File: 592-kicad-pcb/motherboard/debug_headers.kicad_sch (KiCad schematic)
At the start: 7 parts, among them J4 Conn_02x06_Odd_Even, J5 Conn_02x06_Odd_Even, J7 Conn_02x06_Odd_Even, J8 Conn_02x06_Odd_Even, J9 Conn_02x06_Odd_Even

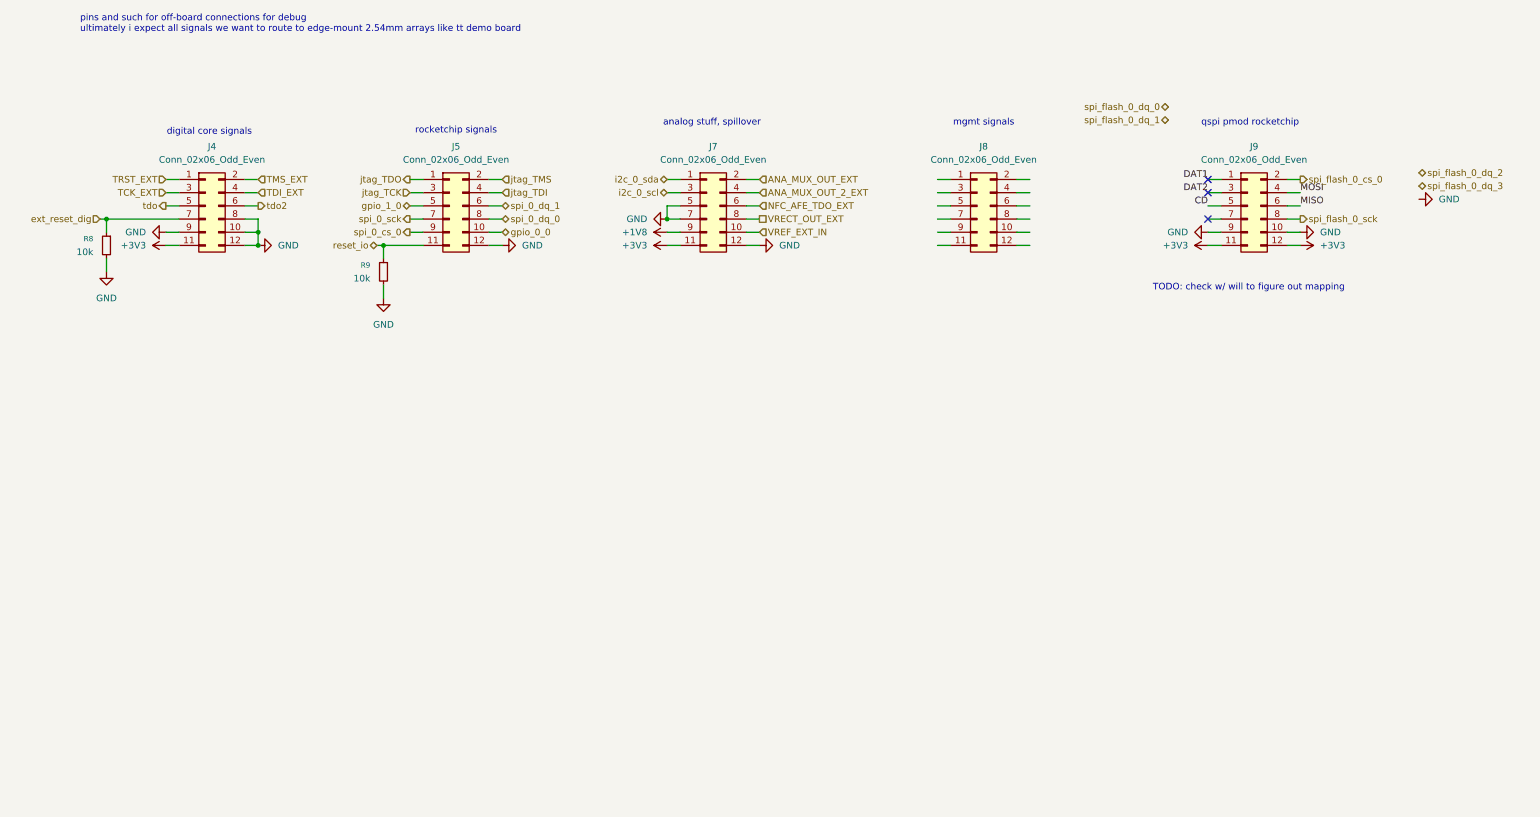
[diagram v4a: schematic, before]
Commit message: clean up some pull up/downs
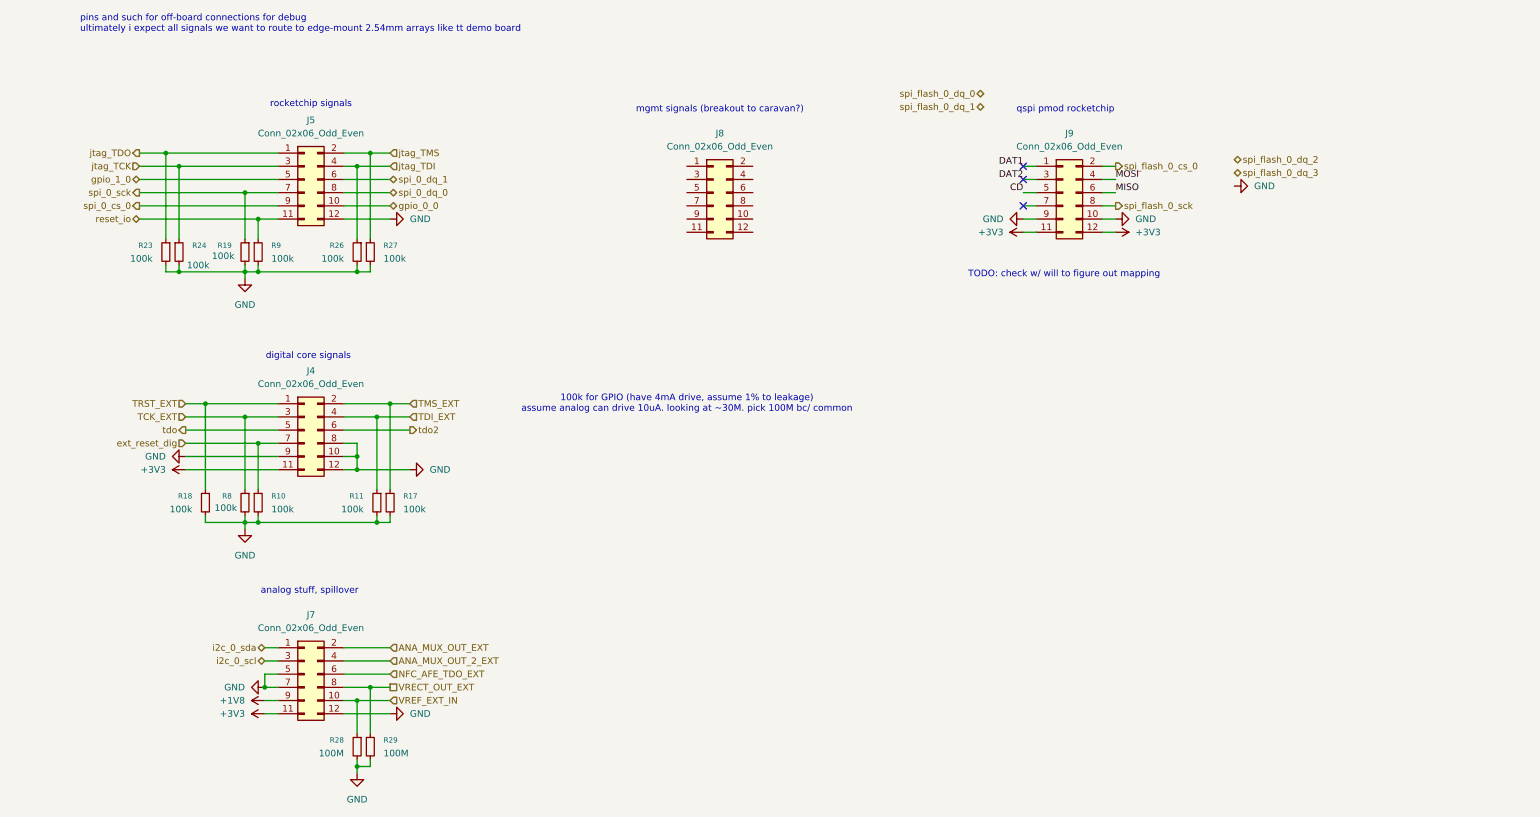
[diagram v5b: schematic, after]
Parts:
- added R10, R11, R17, R18, R19, R23, R24, R26, R27: 100k, Capacitor_SMD:C_0603_1608Metric, symbol Device:R_Small
- added R28, R29: 100M, Capacitor_SMD:C_0603_1608Metric, symbol Device:R_Small
- R8, R9: value 10k -> 100k
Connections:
- net GND: now also R10.2, R11.2, R17.2, R18.2, R19.2, R23.2, R24.2, R26.2, R27.2, R28.2, R29.2
- net TCK_EXT: now also R8.1
- net TDI_EXT: now also R11.1
- net TMS_EXT: now also R17.1
- net TRST_EXT: now also R18.1
- net VRECT_OUT_EXT: now also R29.1
- net VREF_EXT_IN: now also R28.1
- net ext_reset_dig: now also R10.1; no longer R8.1
- net jtag_TCK: now also R24.1
- net jtag_TDI: now also R26.1
- net jtag_TDO: now also R23.1
- net jtag_TMS: now also R27.1
- net spi_0_sck: now also R19.1
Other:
- note added: "100k for GPIO (have 4mA drive, assume 1% to leakage) assume analog can drive 10uA. looking at ~30M. pick 100M bc/ common"
- note added: "mgmt signals (breakout to caravan?)"
- note removed: "mgmt signals"
- moved on the sheet: J4, J5, J7, J8, J9

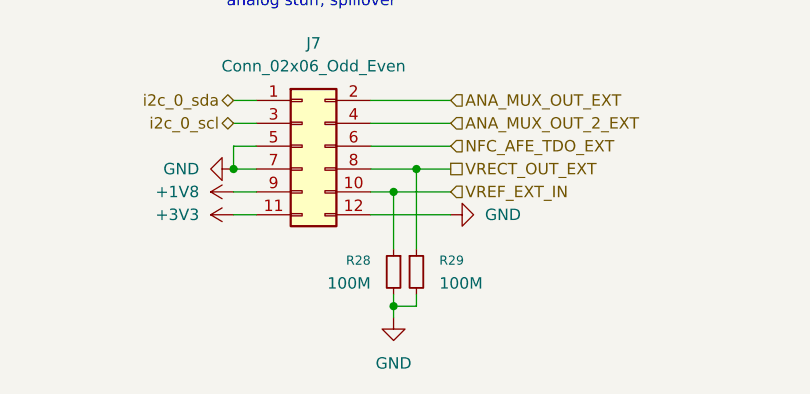
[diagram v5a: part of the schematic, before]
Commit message: add jlc stackup, size pulldowns
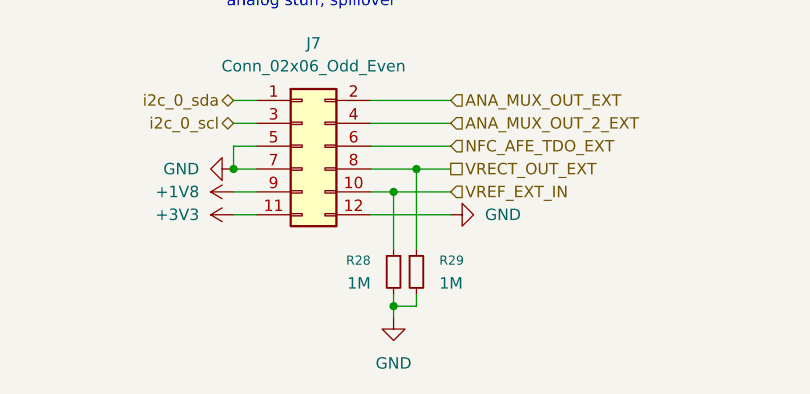
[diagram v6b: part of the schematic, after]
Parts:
- R10, R11, R17, R18, R19, R23, R24, R26, R27, R8, R9: footprint Capacitor_SMD:C_0603_1608Metric -> Resistor_SMD:R_0603_1608Metric
- R28, R29: value 100M -> 1M; footprint Capacitor_SMD:C_0603_1608Metric -> Resistor_SMD:R_0603_1608Metric
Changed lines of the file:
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@@
 			)
 		)
-		(property "Footprint" "Capacitor_SMD:C_0603_1608Metric"
+		(property "Footprint" "Resistor_SMD:R_0603_1608Metric"
 			(at 85.09 110.49 0)
 			(effects
@@
 			)
 		)
-		(property "Footprint" "Capacitor_SMD:C_0603_1608Metric"
+		(property "Footprint" "Resistor_SMD:R_0603_1608Metric"
 			(at 82.55 110.49 0)
 			(effects
@@
 			)
 		)
-		(property "Footprint" "Capacitor_SMD:C_0603_1608Metric"
+		(property "Footprint" "Resistor_SMD:R_0603_1608Metric"
 			(at 41.91 62.23 0)
 			(effects
@@
 			)
 		)
-		(property "Footprint" "Capacitor_SMD:C_0603_1608Metric"
+		(property "Footprint" "Resistor_SMD:R_0603_1608Metric"
 			(at 59.69 110.49 0)
 			(effects
@@
 			)
 		)
-		(property "Footprint" "Capacitor_SMD:C_0603_1608Metric"
+		(property "Footprint" "Resistor_SMD:R_0603_1608Metric"
 			(at 81.28 62.23 0)
 			(effects
@@
 			)
 		)
-		(property "Footprint" "Capacitor_SMD:C_0603_1608Metric"
+		(property "Footprint" "Resistor_SMD:R_0603_1608Metric"
 			(at 78.74 62.23 0)
 			(effects
@@
 			)
 		)
-		(property "Footprint" "Capacitor_SMD:C_0603_1608Metric"
+		(property "Footprint" "Resistor_SMD:R_0603_1608Metric"
 			(at 44.45 62.23 0)
 			(effects
@@
 			)
 		)
-		(property "Footprint" "Capacitor_SMD:C_0603_1608Metric"
+		(property "Footprint" "Resistor_SMD:R_0603_1608Metric"
 			(at 57.15 62.23 0)
 			(effects
@@
 			)
 		)
-		(property "Value" "100M"
+		(property "Value" "1M"
 			(at 83.82 158.7499 0)
 			(effects
@@
 			)
 		)
-		(property "Footprint" "Capacitor_SMD:C_0603_1608Metric"
+		(property "Footprint" "Resistor_SMD:R_0603_1608Metric"
 			(at 81.28 157.48 0)
 			(effects
@@
 			)
 		)
-		(property "Footprint" "Capacitor_SMD:C_0603_1608Metric"
+		(property "Footprint" "Resistor_SMD:R_0603_1608Metric"
 			(at 57.15 110.49 0)
 			(effects
@@
 			)
 		)
-		(property "Footprint" "Capacitor_SMD:C_0603_1608Metric"
+		(property "Footprint" "Resistor_SMD:R_0603_1608Metric"
 			(at 49.53 110.49 0)
 			(effects
@@
 			)
 		)
-		(property "Value" "100M"
+		(property "Value" "1M"
 			(at 76.2 158.7499 0)
 			(effects
@@
 			)
 		)
-		(property "Footprint" "Capacitor_SMD:C_0603_1608Metric"
+		(property "Footprint" "Resistor_SMD:R_0603_1608Metric"
 			(at 78.74 157.48 0)
 			(effects
@@
 			)
 		)
-		(property "Footprint" "Capacitor_SMD:C_0603_1608Metric"
+		(property "Footprint" "Resistor_SMD:R_0603_1608Metric"
 			(at 59.69 62.23 0)
 			(effects

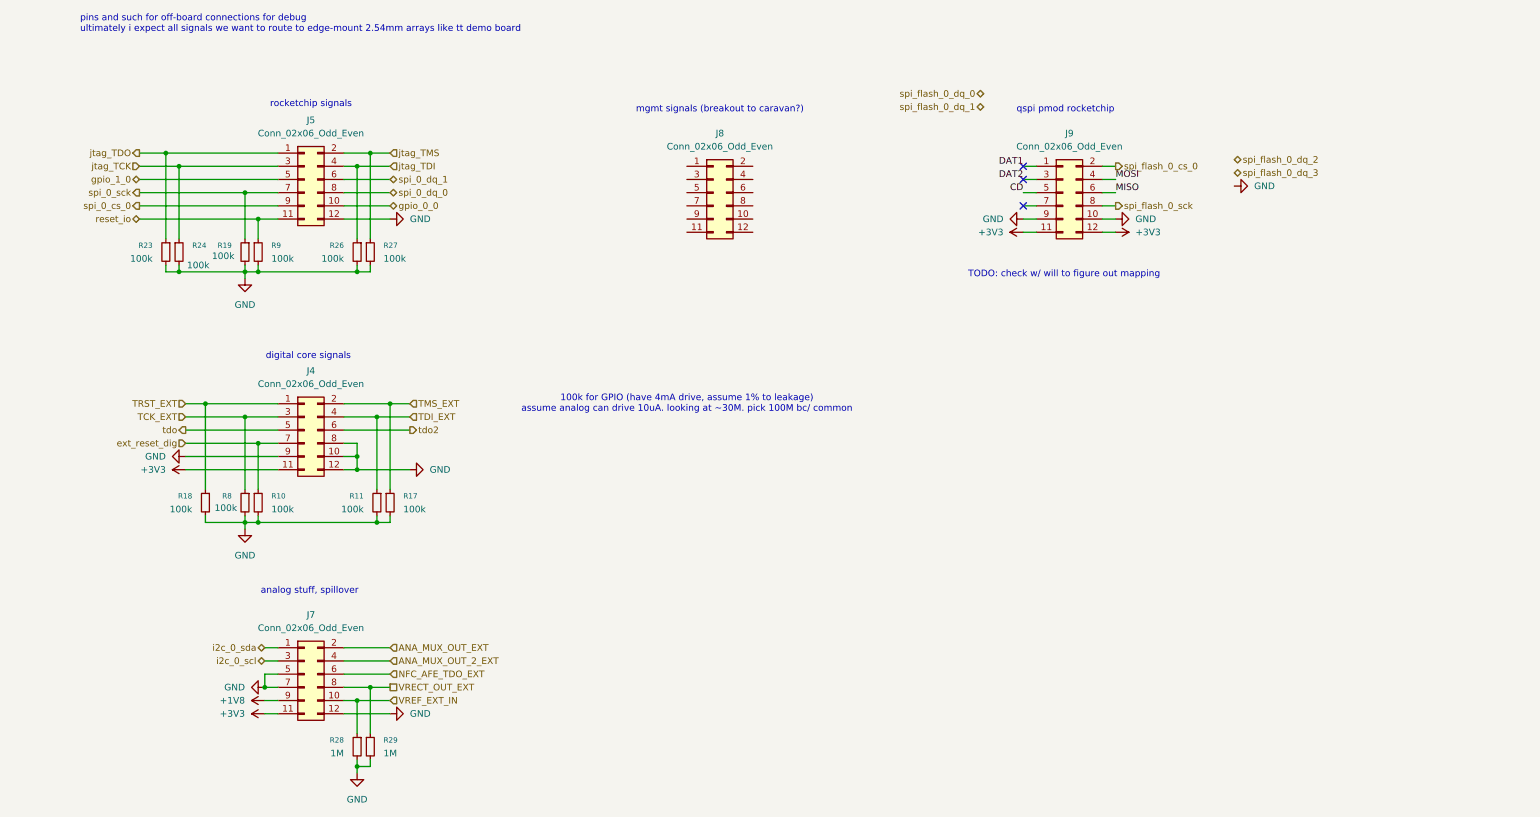
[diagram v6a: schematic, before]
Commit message: clean up schematics, add proper connectors
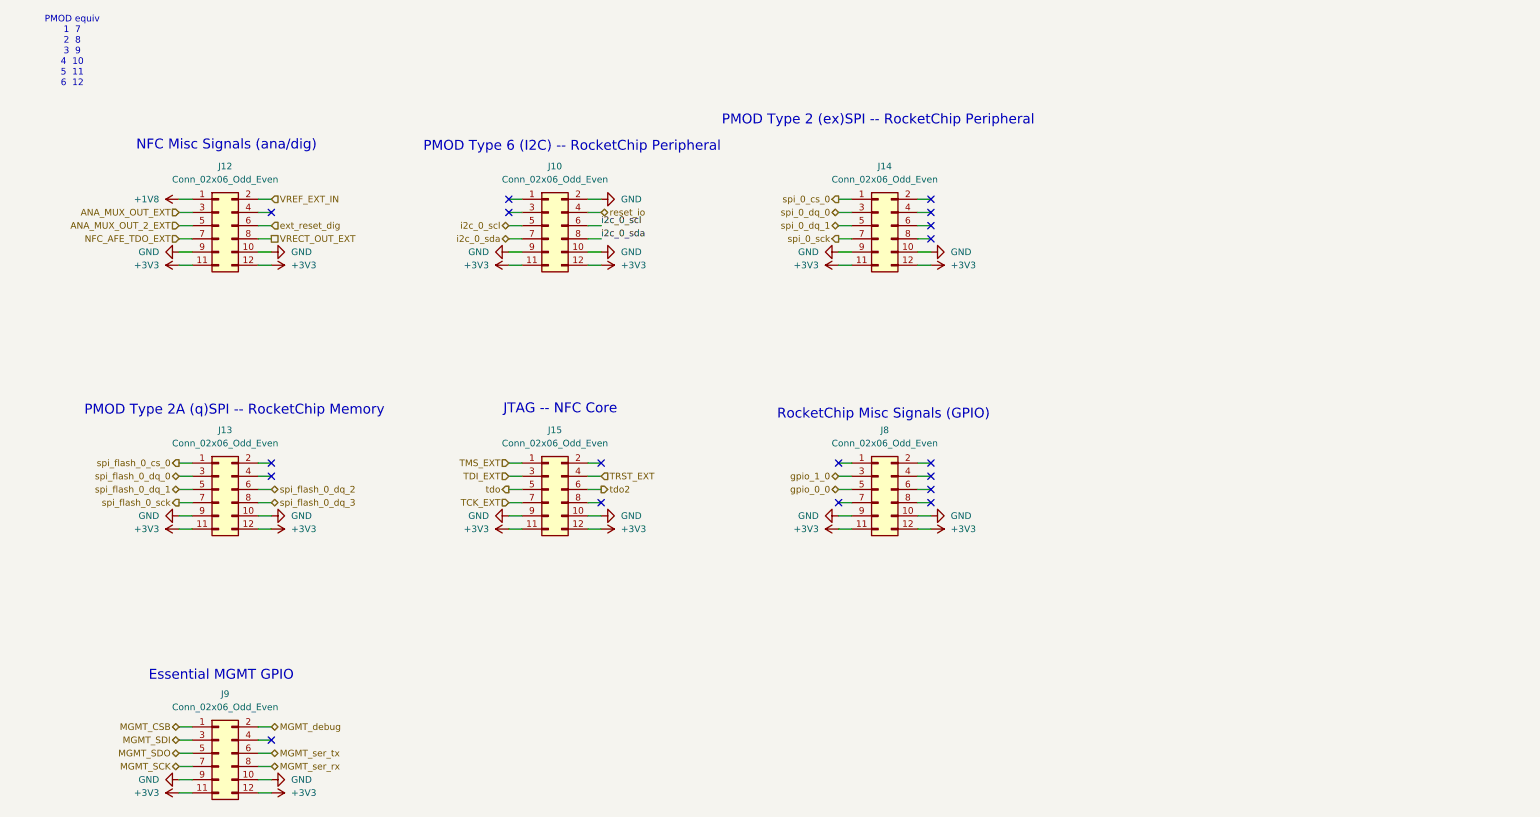
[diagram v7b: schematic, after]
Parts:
- removed J4, J5, J7: Conn_02x06_Odd_Even, Connector_PinSocket_2.54mm:PinSocket_2x06_P2.54mm_Horizontal, symbol Connector_Generic:Conn_02x06_Odd_Even
- removed R10, R11, R17, R18, R19, R23, R24, R26, R27, R8, R9: 100k, Resistor_SMD:R_0603_1608Metric, symbol Device:R_Small
- removed R28, R29: 1M, Resistor_SMD:R_0603_1608Metric, symbol Device:R_Small
- added J10, J12, J13, J14, J15: Conn_02x06_Odd_Even, Connector_PinSocket_2.54mm:PinSocket_2x06_P2.54mm_Horizontal, symbol Connector_Generic:Conn_02x06_Odd_Even
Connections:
- net +1V8: now also J12.1 (Pin_1)
- net +3V3: now also J8.11 (Pin_11), J8.12 (Pin_12), J10.11 (Pin_11), J10.12 (Pin_12), J12.11 (Pin_11), J12.12 (Pin_12), J13.11 (Pin_11), J13.12 (Pin_12), J14.11 (Pin_11), J14.12 (Pin_12), J15.11 (Pin_11), J15.12 (Pin_12)
- net ANA_MUX_OUT_2_EXT: now also J12.5 (Pin_5)
- net ANA_MUX_OUT_EXT: now also J12.3 (Pin_3)
- net GND: now also J8.10 (Pin_10), J8.9 (Pin_9), J10.10 (Pin_10), J10.2 (Pin_2), J10.9 (Pin_9), J12.10 (Pin_10), J12.9 (Pin_9), J13.10 (Pin_10), J13.9 (Pin_9), J14.10 (Pin_10), J14.9 (Pin_9), J15.10 (Pin_10), J15.9 (Pin_9)
- net NFC_AFE_TDO_EXT: now also J12.7 (Pin_7)
- net TCK_EXT: now also J15.7 (Pin_7)
- net TDI_EXT: now also J15.3 (Pin_3)
- net TMS_EXT: now also J15.1 (Pin_1)
- net TRST_EXT: now also J15.4 (Pin_4)
- net VRECT_OUT_EXT: now also J12.8 (Pin_8)
- net VREF_EXT_IN: now also J12.2 (Pin_2)
- net ext_reset_dig: now also J12.6 (Pin_6)
- net gpio_0_0: now also J8.5 (Pin_5)
- net gpio_1_0: now also J8.3 (Pin_3)
- net i2c_0_scl: now also J10.5 (Pin_5), J10.6 (Pin_6)
- net i2c_0_sda: now also J10.7 (Pin_7), J10.8 (Pin_8)
- net reset_io: now also J10.4 (Pin_4)
- net spi_0_cs_0: now also J14.1 (Pin_1)
- net spi_0_dq_0: now also J14.3 (Pin_3)
- net spi_0_dq_1: now also J14.5 (Pin_5)
- net spi_0_sck: now also J14.7 (Pin_7)
- net spi_flash_0_cs_0: now also J13.1 (Pin_1); no longer J9.2 (Pin_2)
- net spi_flash_0_dq_0: now also J13.3 (Pin_3)
- net spi_flash_0_dq_1: now also J13.5 (Pin_5)
- net spi_flash_0_dq_2: now also J13.6 (Pin_6)
- net spi_flash_0_dq_3: now also J13.8 (Pin_8)
- net spi_flash_0_sck: now also J13.7 (Pin_7); no longer J9.8 (Pin_8)
- net tdo: now also J15.5 (Pin_5)
- net tdo2: now also J15.6 (Pin_6)
- net MGMT_SCK: now reaches J9.7 (Pin_7)
- net CD renamed MGMT_SDO
- net DAT1 renamed MGMT_CSB
- net DAT2 renamed MGMT_SDI
- net MISO renamed MGMT_ser_tx
- net MOSI: no longer names the net of J9.4 (Pin_4)
- new net MGMT_debug: J9.2 (Pin_2)
- new net MGMT_ser_rx: J9.8 (Pin_8)
- no-connect marks 3 -> 18
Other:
- note added: "Essential MGMT GPIO"
- note added: "JTAG -- NFC Core"
- note added: "NFC Misc Signals (ana/dig)"
- note added: "PMOD Type 2 (ex)SPI -- RocketChip Peripheral"
- note added: "PMOD Type 2A (q)SPI -- RocketChip Memory"
- note added: "PMOD Type 6 (I2C) -- RocketChip Peripheral"
- note added: "PMOD equiv 1 7 2 8 3 9 4 10 5 11 6 12"
- note added: "RocketChip Misc Signals (GPIO)"
- note removed: "100k for GPIO (have 4mA drive, assume 1% to leakage) assume analog can drive 10uA. looking at ~30M. pick 100M bc/ common"
- note removed: "TODO: check w/ will to figure out mapping"
- note removed: "analog stuff, spillover"
- note removed: "digital core signals"
- note removed: "mgmt signals (breakout to caravan?)"
- note removed: "pins and such for off-board connections for debug ultimately i expect all signals we want to route to edge-mount 2.54mm arrays like tt demo board"
- note removed: "qspi pmod rocketchip"
- note removed: "rocketchip signals"
